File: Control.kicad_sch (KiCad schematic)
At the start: 0 parts

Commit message: Created a page for BAT eFuse and current sensing. Updated the cControl page with part of the harware cutoff
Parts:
- added C79, C80: 10nF, symbol Device:C
- added C81, C82, C83: 100nF, symbol Device:C
- added NT3: NetTie_2, symbol Device:NetTie_2
- added R_BOT, R_BOT1: 180k, symbol Device:R
- added R_BOT2, R_BOT3, R_PUP, R_PUP2, R_PUP3: 10k, symbol Device:R
- added R_FILT: 402, symbol Device:R
- added R_FILT2: 2.61k, symbol Device:R
- added R_IN: 100, symbol Device:R
- added R_TOP, R_TOP1: 39k, symbol Device:R
- added R_TOP2: 11.5k, symbol Device:R
- added R_TOP3: 3.2k, symbol Device:R
- added R_hyst, R_hyst1: 1MOhm, symbol Device:R
- added U2: LT6108IMS8-1-TRPBF, MSOP-8_MS_LIT, symbol PULSE_Library:LT6108IMS8-1-TRPBF
- added U3: LM139ADRG4, D14, symbol PULSE_Library:LM139ADRG4
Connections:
- new net: R_IN.1, U2.8 (SENSEHI)
- new net: R_FILT.1, R_FILT2.2, U2.5 (INC)
- new net: R_BOT3.2, R_TOP3.1, U3.4 (2IN-)
- new net: R_BOT2.2, R_TOP2.1, U3.6 (1IN-)
- new net 3.3V: C82.1, R_PUP.1, R_PUP2.1, R_PUP3.2, R_TOP2.2, R_TOP3.2, U2.2 (EN/*RST), U3.3 (VCC)
- new net BAT_OVP: R_PUP2.2, R_PUP3.1, R_hyst.1, R_hyst1.1, U3.1 (1OUT), U3.2 (2OUT)
- new net BAT_SHUNT_IN: R_IN.2, U2.7 (V+)
- new net BAT_SHUNT_OUT: U2.1 (SENSELO)
- new net BUCK_OUT: R_TOP.1
- new net GND: C79.2, C80.2, C81.2, C82.2, C83.2, NT3.1, NT3.2, R_BOT.1, R_BOT1.1, R_BOT2.1, R_BOT3.1, R_FILT2.1, U2.4 (V-), U3.12 (GND)
- new net I_BAT_ANA: C81.1, R_FILT.2, U2.6 (OUTA)
- new net OCV_FLAG: R_PUP.2, U2.3 (OUTC)
- new net PVIN: R_TOP1.1
- new net VBAT_SENSE: C79.1, C83.1, R_BOT.2, R_TOP.2, R_hyst.2, U3.7 (1IN+)
- new net VPANNEL_SENSE: C80.1, R_BOT1.2, R_TOP1.2, R_hyst1.2, U3.5 (2IN+)

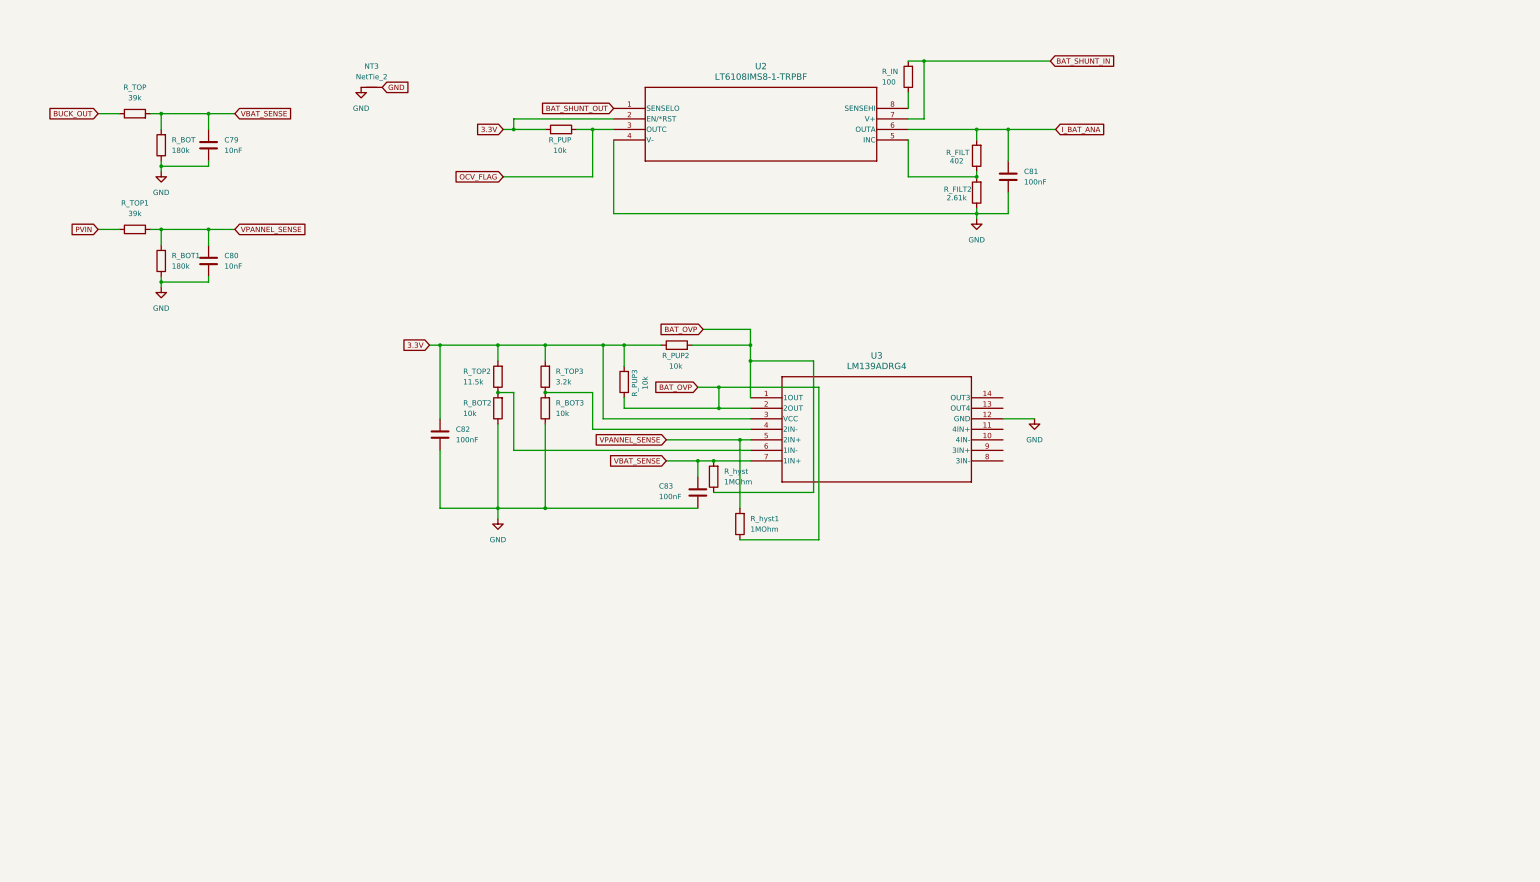
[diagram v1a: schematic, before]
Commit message: Created a page for PANNEL efuse, modifiel all to local labels, functionally finished
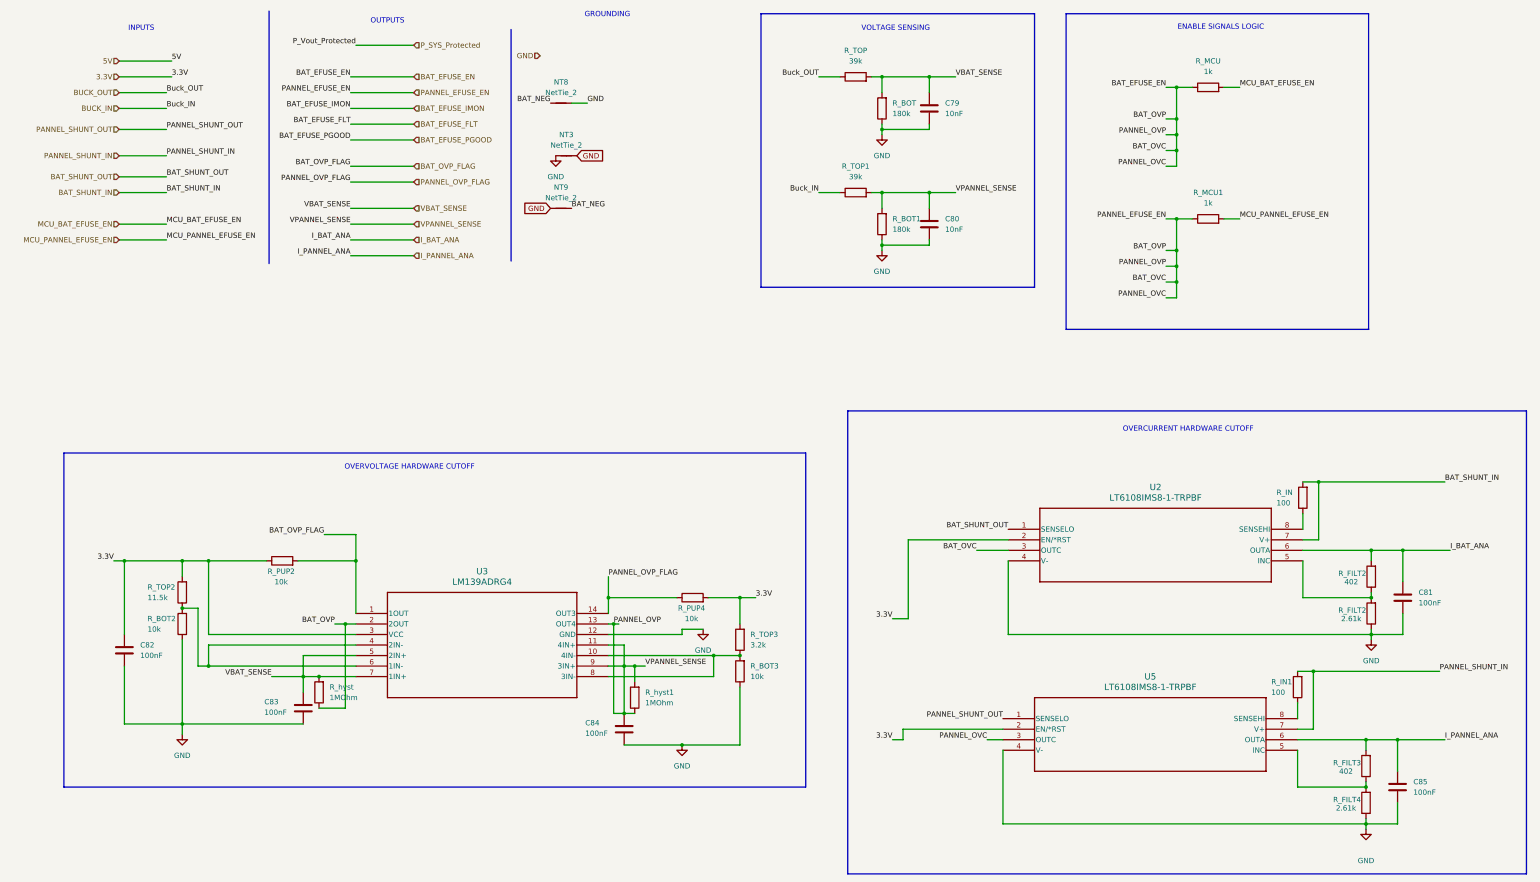
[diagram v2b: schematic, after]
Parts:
- removed R_FILT: 402, symbol Device:R
- removed R_PUP, R_PUP3: 10k, symbol Device:R
- added C84, C85: 100nF, symbol Device:C
- added NT8, NT9: NetTie_2, symbol Device:NetTie_2
- added R_FILT2, R_FILT3: 402, symbol Device:R
- added R_FILT4: 2.61k, symbol Device:R
- added R_IN1: 100, symbol Device:R
- added R_MCU, R_MCU1: 1k, symbol Device:R
- added R_PUP4: 10k, symbol Device:R
- added U5: LT6108IMS8-1-TRPBF, MSOP-8_MS_LIT, symbol PULSE_Library:LT6108IMS8-1-TRPBF
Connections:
- net OCV_FLAG is gone; now on net BAT_EFUSE_EN: U2.3 (OUTC)
- net 3.3V: now also R_PUP4.2, U5.2 (EN/*RST)
- net GND: now also C84.2, C85.2, NT8.2, NT9.1, R_FILT4.1, U5.4 (V-)
- net I_BAT_ANA: now also R_FILT2.2
- net VBAT_SENSE: now also U3.5 (2IN+)
- net at R_FILT2.2, U2.5 (INC): now also R_FILT2.1
- net at R_BOT3.2, R_TOP3.1: now also U3.10 (4IN-), U3.8 (3IN-); no longer U3.4 (2IN-)
- net at R_BOT2.2, R_TOP2.1, U3.6 (1IN-): now also U3.4 (2IN-)
- net BAT_EFUSE_EN: now reaches U3.11 (4IN+)
- net BAT_EFUSE_EN: now also C80.1, R_BOT1.2, R_TOP1.2, R_hyst.1, R_hyst1.1, R_hyst1.2, U3.13 (OUT4), U3.2 (2OUT), U3.9 (3IN+), C84.1, R_MCU.1, R_MCU1.1, U5.3 (OUTC)
- net PANNEL_OVP_FLAG: now reaches U3.14 (OUT3)
- net PANNEL_OVP_FLAG: now also R_PUP4.1
- removed net BAT_OVP: R_PUP2.2, R_hyst.1, R_hyst1.1, U3.1 (1OUT), U3.2 (2OUT)
- net PVIN renamed BUCK_IN
- removed net VPANNEL_SENSE: C80.1, R_BOT1.2, R_TOP1.2, R_hyst1.2, U3.5 (2IN+)
- new net: R_IN1.1, U5.8 (SENSEHI)
- new net: R_FILT3.1, R_FILT4.2, U5.5 (INC)
- new net BAT_NEG: NT8.1, NT9.2
- new net BAT_OVP_FLAG: R_PUP2.2, U3.1 (1OUT)
- new net I_PANNEL_ANA: C85.1, R_FILT3.2, U5.6 (OUTA)
- new net MCU_BAT_EFUSE_EN: R_MCU.2
- new net MCU_PANNEL_EFUSE_EN: R_MCU1.2
- new net PANNEL_SHUNT_IN: R_IN1.2, U5.7 (V+)
- new net PANNEL_SHUNT_OUT: U5.1 (SENSELO)
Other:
- note added: "ENABLE SIGNALS LOGIC"
- note added: "GROUNDING"
- note added: "INPUTS"
- note added: "OUTPUTS"
- note added: "OVERCURRENT HARDWARE CUTOFF"
- note added: "OVERVOLTAGE HARDWARE CUTOFF"
- note added: "VOLTAGE SENSING"
- moved on the sheet: C79, C80, C81, C82, C83, NT3, R_BOT, R_BOT1, R_BOT2, R_BOT3, R_FILT2, R_IN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

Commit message: Some edits
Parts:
- removed NT3, NT8, NT9: NetTie_2, symbol Device:NetTie_2
- removed R_MCU1: 1k, symbol Device:R
- added D18, D19, D20, D21, D22, D23: 1N4148WT, Diode_SMD:D_SOD-523, symbol Diode:1N4148WT
- added R_BOT5: 180k, symbol Device:R
- added R_MCU2: 1k, symbol Device:R
- added R_PD, R_PD1: 100k, symbol Device:R
- added R_PUP6: 10k, symbol Device:R
- added R_TOP5: 247k, symbol Device:R
- added R_hyst2: 1MOhm, symbol Device:R
- R_BOT2, R_BOT3: value 10k -> 180k
- R_TOP, R_TOP1: value 39k -> 680k
- R_TOP2: value 11.5k -> 147k
- R_TOP3: value 3.2k -> 68k
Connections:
- net 3.3V: now also R_PUP6.1, R_TOP5.2
- net BAT_EFUSE_EN: now also D18.2 (A), D19.2 (A), D20.2 (A), R_PD.2; no longer C80.1, C84.1, R_BOT1.2, R_TOP1.2, R_hyst.1, R_hyst1.1, R_hyst1.2, U2.3 (OUTC), U3.11 (4IN+), U3.13 (OUT4), U3.2 (2OUT), U3.9 (3IN+), U5.3 (OUTC)
- net BAT_OVP_FLAG: now also R_hyst.2, U3.2 (2OUT), D18.1 (K), D21.1 (K); no longer U3.1 (1OUT)
- net GND: now also R_BOT5.1, R_PD.1, R_PD1.1
- net MCU_PANNEL_EFUSE_EN: now also R_MCU2.2
- net PANNEL_OVP_FLAG: now also R_hyst1.2, D22.1 (K)
- net VBAT_SENSE: now also R_hyst.1, U3.6 (1IN-), R_hyst2.1; no longer R_hyst.2, U3.7 (1IN+)
- net at R_BOT3.2, R_TOP3.1, U3.8 (3IN-): no longer U3.10 (4IN-)
- net at R_BOT2.2, R_TOP2.1, U3.4 (2IN-): no longer U3.6 (1IN-)
- new net: R_BOT5.2, R_TOP5.1, U3.7 (1IN+)
- new net BAT_OVC: D20.1 (K), U2.3 (OUTC)
- new net BAT_UVP_FLAG: D19.1 (K), R_PUP6.2, R_hyst2.2, U3.1 (1OUT)
- new net PANNEL_EFUSE_EN: D21.2 (A), D22.2 (A), D23.2 (A), R_MCU2.1, R_PD1.2
- new net PANNEL_OVC: D23.1 (K), U5.3 (OUTC)
- new net VPANNEL_SENSE: C80.1, C84.1, R_BOT1.2, R_TOP1.2, R_hyst1.1, U3.9 (3IN+)
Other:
- moved on the sheet: C82, C83, R_MCU, R_PUP2, R_hyst, R_hyst1

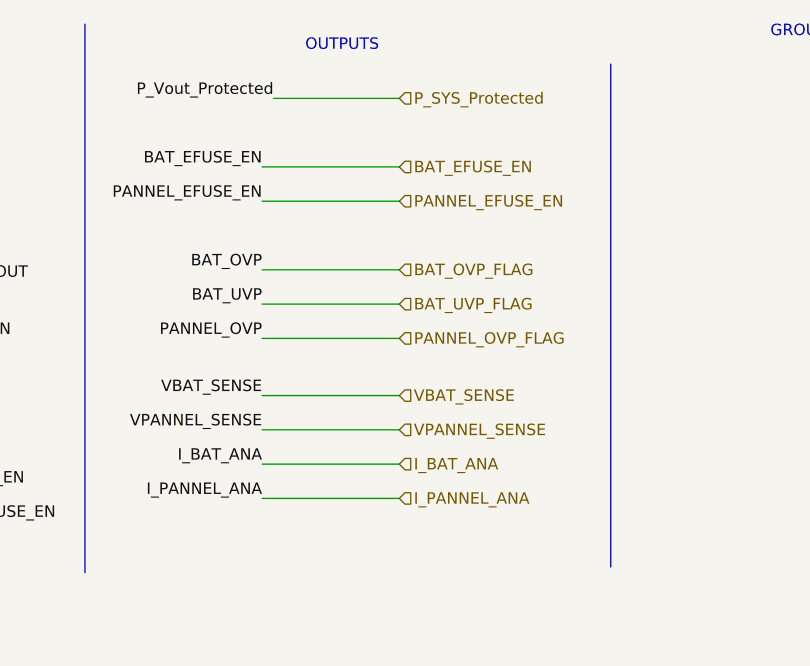
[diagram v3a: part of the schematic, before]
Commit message: Modification of ROOT sheet blocks
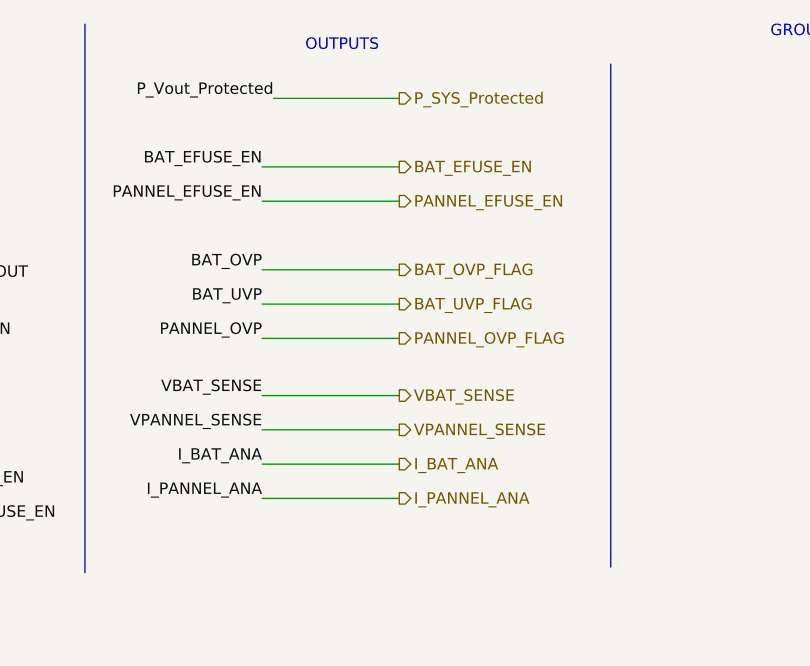
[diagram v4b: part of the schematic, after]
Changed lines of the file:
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@@
 	)
 	(hierarchical_label "BAT_UVP_FLAG"
-		(shape input)
+		(shape output)
 		(at 110.49 45.72 0)
 		(effects
@@
 	)
 	(hierarchical_label "VBAT_SENSE"
-		(shape input)
+		(shape output)
 		(at 110.49 55.88 0)
 		(effects
@@
 	)
 	(hierarchical_label "BAT_EFUSE_EN"
-		(shape input)
+		(shape output)
 		(at 110.49 30.48 0)
 		(effects
@@
 	)
 	(hierarchical_label "P_SYS_Protected"
-		(shape input)
+		(shape output)
 		(at 110.49 22.86 0)
 		(effects
@@
 	)
 	(hierarchical_label "PANNEL_OVP_FLAG"
-		(shape input)
+		(shape output)
 		(at 110.49 49.53 0)
 		(effects
@@
 	)
 	(hierarchical_label "BAT_OVP_FLAG"
-		(shape input)
+		(shape output)
 		(at 110.49 41.91 0)
 		(effects
@@
 	)
 	(hierarchical_label "PANNEL_EFUSE_EN"
-		(shape input)
+		(shape output)
 		(at 110.49 34.29 0)
 		(effects
@@
 	)
 	(hierarchical_label "I_BAT_ANA"
-		(shape input)
+		(shape output)
 		(at 110.49 63.5 0)
 		(effects
@@
 	)
 	(hierarchical_label "I_PANNEL_ANA"
-		(shape input)
+		(shape output)
 		(at 110.49 67.31 0)
 		(effects
@@
 	)
 	(hierarchical_label "VPANNEL_SENSE"
-		(shape input)
+		(shape output)
 		(at 110.49 59.69 0)
 		(effects

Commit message: lastest
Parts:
- removed C81, C84, C85: 100nF, symbol Device:C
- added C81, C84, C85: 100nF, Capacitor_SMD:C_0603_1608Metric, symbol PULSE_Library:C0603X6S0J104M030BC
- added C93: 10nF, PULSE_Library:CAPC2012X145N, symbol PULSE_Library:C2012X7R1A106M125AC
- added R_BOT8: 180k, Resistor_SMD:R_0603_1608Metric, symbol Device:R
- added R_BYPASS2, R_BYPASS3, R_BYPASS4, R_BYPASS5, R_BYPASS6, R_BYPASS7: 0, Resistor_SMD:R_0603_1608Metric, symbol Device:R
- added R_TOP8: 680k, Resistor_SMD:R_0603_1608Metric, symbol Device:R
- added TP10: VBAT_SENSE, TestPoint:TestPoint_Pad_D2.0mm, symbol Connector:TestPoint_Probe
- added TP11: BAT_EFUSE_EN, TestPoint:TestPoint_Pad_D2.0mm, symbol Connector:TestPoint_Probe
- added TP12: PANNEL_EFUSE_EN, TestPoint:TestPoint_Pad_D2.0mm, symbol Connector:TestPoint_Probe
- added TP13: MCU_BAT_EFUSE_EN, TestPoint:TestPoint_Pad_D2.0mm, symbol Connector:TestPoint_Probe
- added TP14: MCU_PANNEL_EFUSE_EN, TestPoint:TestPoint_Pad_D2.0mm, symbol Connector:TestPoint_Probe
- added TP15: BAT_UVP, TestPoint:TestPoint_Pad_D2.0mm, symbol Connector:TestPoint_Probe
- added TP16: BAT_OVP, TestPoint:TestPoint_Pad_D2.0mm, symbol Connector:TestPoint_Probe
- added TP17: PANNEL_OVP, TestPoint:TestPoint_Pad_D2.0mm, symbol Connector:TestPoint_Probe
- added TP18: BAT_SHUNT_OUT, TestPoint:TestPoint_Pad_D2.0mm, symbol Connector:TestPoint_Probe
- added TP19: BAT_SHUNT_IN, TestPoint:TestPoint_Pad_D2.0mm, symbol Connector:TestPoint_Probe
- added TP20: PANNEL_SHUNT_OUT, TestPoint:TestPoint_Pad_D2.0mm, symbol Connector:TestPoint_Probe
- added TP21: PANNEL_SHUNT_IN, TestPoint:TestPoint_Pad_D2.0mm, symbol Connector:TestPoint_Probe
- added TP8: VPANNEL_SENSE, TestPoint:TestPoint_Pad_D2.0mm, symbol Connector:TestPoint_Probe
- added TP9: VCHG_RAIL_SENSE, TestPoint:TestPoint_Pad_D2.0mm, symbol Connector:TestPoint_Probe
- C79, C80: footprint (none) -> PULSE_Library:CAPC2012X145N; symbol Device:C -> PULSE_Library:C2012X7R1A106M125AC; Height (none) -> 1.45; Manufacturer_Name (none) -> TDK; Manufacturer_Part_Number (none) -> C2012X7R1A106M125AC; Mouser Part Number (none) -> 810-C2012X7R1A106M; Mouser Price/Stock (none) -> https://www.mouser.co.uk/ProductDetail/TDK/C2012X7R1A106M12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
- C82, C83: footprint (none) -> Capacitor_SMD:C_0603_1608Metric; symbol Device:C -> PULSE_Library:C0603X6S0J104M030BC; Height (none) -> 0.33; Manufacturer_Name (none) -> TDK; Manufacturer_Part_Number (none) -> C0603X6S0J104M030BC; Mouser Part Number (none) -> 810-C0603X6S0J104M; Mouser Price/Stock (none) -> https://www.mouser.co.uk/ProductDetail/TDK/C0603X6S0J104M03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
- R_BOT1, R_BOT2, R_BOT3, R_BOT5, R_FILT2, R_FILT3, R_FILT4, R_IN1, R_PD1, R_PUP2, R_PUP4, R_PUP6, R_TOP1, R_TOP2, R_TOP3, R_TOP5, R_hyst1, R_hyst2: footprint (none) -> Resistor_SMD:R_0603_1608Metric
- R_BOT6: renamed from R_BOT; footprint (none) -> Resistor_SMD:R_0603_1608Metric
- R_FILT10: renamed from R_FILT2; footprint (none) -> Resistor_SMD:R_0603_1608Metric
- R_IN2: renamed from R_IN; footprint (none) -> Resistor_SMD:R_0603_1608Metric
- R_MCU_EN1: renamed from R_MCU; footprint (none) -> Resistor_SMD:R_0603_1608Metric
- R_MCU_EN2: renamed from R_MCU2; footprint (none) -> Resistor_SMD:R_0603_1608Metric
- R_PD2: renamed from R_PD; footprint (none) -> Resistor_SMD:R_0603_1608Metric
- R_TOP6: renamed from R_TOP; footprint (none) -> Resistor_SMD:R_0603_1608Metric
- R_hyst3: renamed from R_hyst; footprint (none) -> Resistor_SMD:R_0603_1608Metric
- U2, U5: footprint MSOP-8_MS_LIT -> PULSE_Library:MSOP-8_MS_LIT; Mouser Part Number (none) -> 584-LT6108AIMS8-1PBF; Mouser link (none) -> https://www.mouser.ch/ProductDetail/Analog-Devices/LT6108AI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
- U3: footprint D14 -> Package_DIP:CERDIP-14_W7.62mm_SideBrazed_LongPads_Socket; Mouser Part Number (none) -> 595-LM139DR; Mouser link (none) -> https://www.mouser.ch/ProductDetail/Texas-Instruments/LM139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
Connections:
- net BAT_EFUSE_EN: now also TP11.1
- net BAT_OVC: now also R_BYPASS4.1; no longer D20.1 (K)
- net BAT_OVP_FLAG: now also R_BYPASS2.1, R_BYPASS5.1, TP16.1; no longer D18.1 (K), D21.1 (K)
- net BAT_SHUNT_IN: now also TP19.1
- net BAT_SHUNT_OUT: now also TP18.1
- net BAT_UVP_FLAG: now also R_BYPASS3.1, TP15.1; no longer D19.1 (K)
- net GND: now also C83.1, C81.1, C84.1, C85.1, C93.2, R_BOT8.1; no longer C83.2
- net I_BAT_ANA: now also C81.2
- net I_PANNEL_ANA: now also C85.2
- net MCU_BAT_EFUSE_EN: now also TP13.1
- net MCU_PANNEL_EFUSE_EN: now also TP14.1
- net PANNEL_EFUSE_EN: now also TP12.1
- net PANNEL_OVC: now also R_BYPASS7.1; no longer D23.1 (K)
- net PANNEL_OVP_FLAG: now also R_BYPASS6.1, TP17.1; no longer D22.1 (K)
- net PANNEL_SHUNT_IN: now also TP21.1
- net PANNEL_SHUNT_OUT: now also TP20.1
- net VBAT_SENSE: now also C83.2, C93.1, R_BOT8.2, R_TOP8.2, TP10.1; no longer C79.1, C83.1, R_BOT6.2, R_TOP6.2
- net VPANNEL_SENSE: now also C84.2, TP8.1
- new net: D18.1 (K), R_BYPASS2.2
- new net: D19.1 (K), R_BYPASS3.2
- new net: D20.1 (K), R_BYPASS4.2
- new net: D23.1 (K), R_BYPASS7.2
- new net: D22.1 (K), R_BYPASS6.2
- new net: D21.1 (K), R_BYPASS5.2
- new net VBAT: R_TOP8.1
- new net VCHG_RAIL_SENSE: C79.1, R_BOT6.2, R_TOP6.2, TP9.1
- no-connect marks 0 -> 3
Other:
- moved on the sheet: D21, D22, D23, R_BOT1, R_BOT6, R_MCU_EN2, R_PD1, R_TOP1, R_TOP6, U3
